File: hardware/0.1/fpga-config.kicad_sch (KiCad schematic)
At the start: 37 parts, among them J2 JTAG, J5 USB_C_Receptacle_USB2.0, Q1 BSS138, SW1 SW_Push, U1 ECP5U_12_CABGA256, U4 USBLC6-2SC6, U6 W25Q128JVSIQ

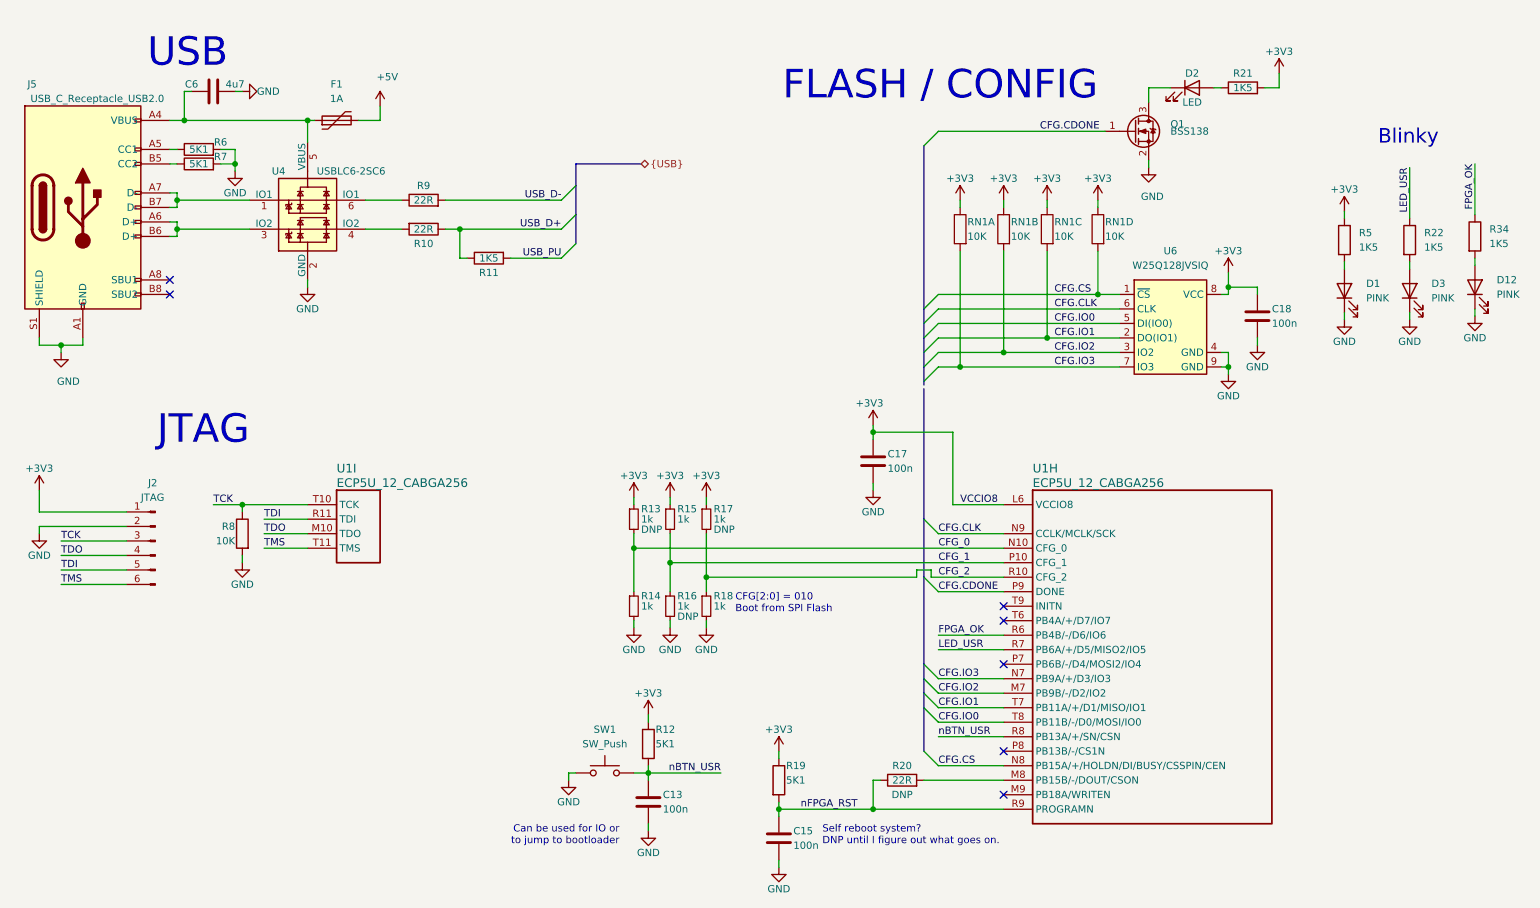
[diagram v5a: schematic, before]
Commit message: half IO laid out
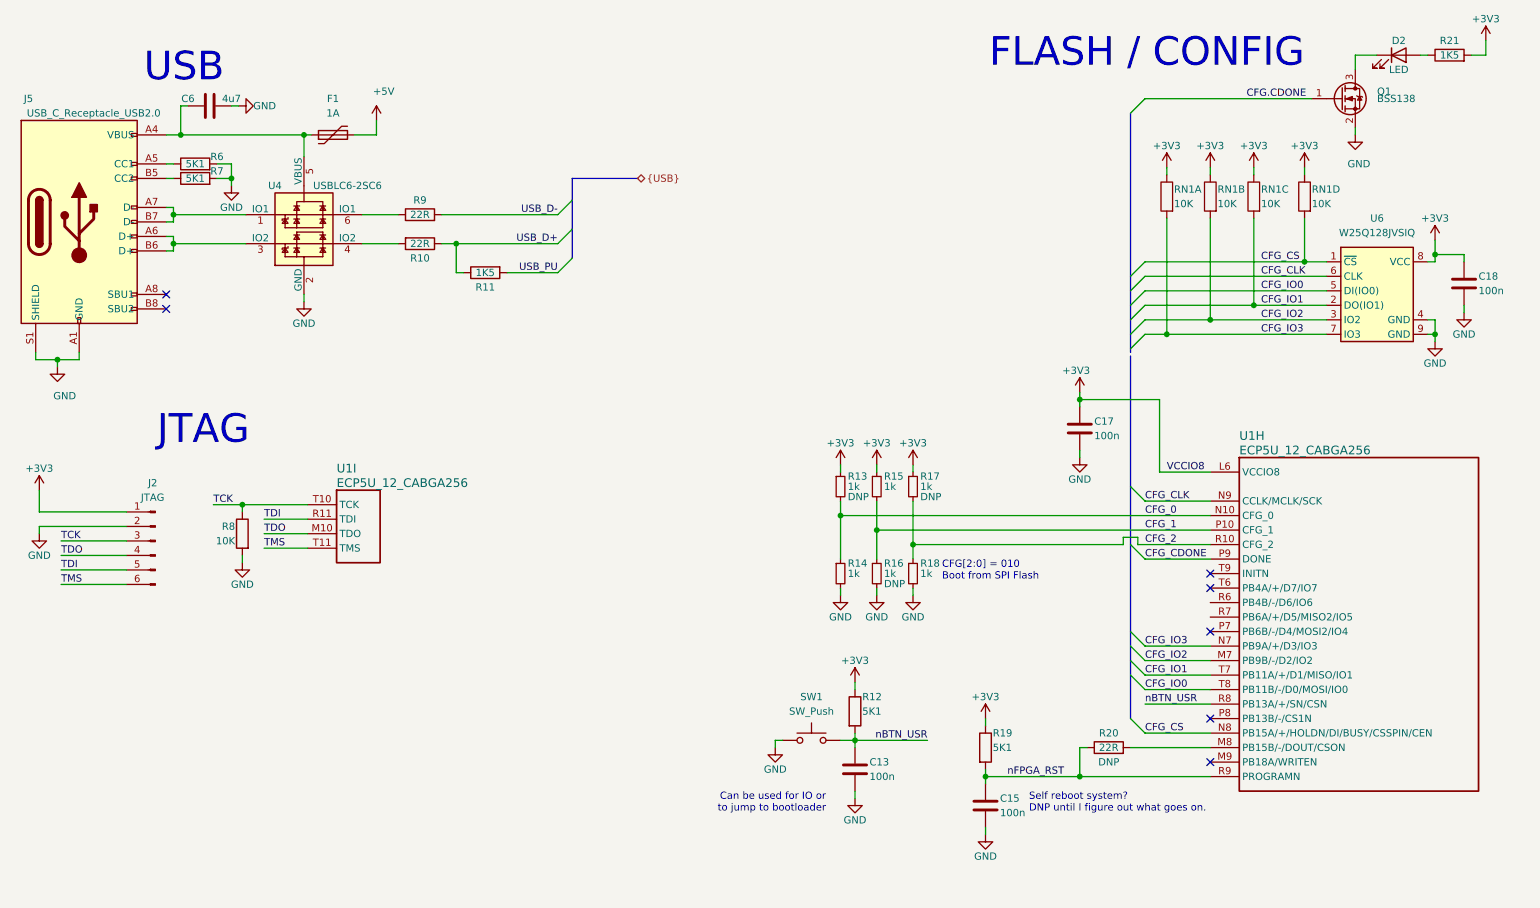
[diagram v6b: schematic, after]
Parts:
- removed D1, D12, D3: PINK, LED_SMD:LED_0603_1608Metric, symbol Device:LED
- removed R22, R34, R5: 1K5, Resistor_SMD:R_0402_1005Metric, symbol Device:R
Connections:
- net CFG.CDONE: no longer U1.P9 (DONE)
- net CFG.CLK renamed CFG_CLK
- net CFG.CS renamed CFG_CS
- net CFG.IO0 renamed CFG_IO0
- net CFG.IO1 renamed CFG_IO1
- net CFG.IO2 renamed CFG_IO2
- net CFG.IO3 renamed CFG_IO3
- net FPGA_OK: no longer names the net of U1.R6 (PB4B/-/D6/IO6)
- net LED_USR: no longer names the net of U1.R7 (PB6A/+/D5/MISO2/IO5)
- new net CFG_CDONE: U1.P9 (DONE)
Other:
- note removed: "Blinky"
- moved on the sheet: C13, C15, C17, C18, C6, D2, F1, J5, Q1, R10, R11, R12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

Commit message: half IO routed
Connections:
- net CFG.CDONE is gone; now on net CFG_CDONE: Q1.1 (G)
- net CFG_CLK: now also RN1.2
- net CFG_CS: now also RN1.4; no longer RN1.1
- net CFG_IO1: no longer RN1.2
- net CFG_IO3: now also RN1.1; no longer RN1.4
- no-connect marks 7 -> 9
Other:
- moved on the sheet: C13, C15, C17, C18, D2, Q1, R12, R13, R14, R15, R16, R17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
